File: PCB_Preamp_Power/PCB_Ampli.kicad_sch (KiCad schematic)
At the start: 0 parts

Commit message: PCBV3_Preamp_Power
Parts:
- added H1, H2, H3, H4: MountingHole_Pad, MountingHole:MountingHole_3.2mm_M3_Pad_Via, symbol Mechanical:MountingHole_Pad
- added J4: Conn_01x02, Connector_AMASS:AMASS_XT60-M_1x02_P7.20mm_Vertical, symbol Connector_Generic:Conn_01x02
- added SW2: SW_Push_DPDT, Library_f:Holes_Switch_DPDT, symbol Switch:SW_Push_DPDT
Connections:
- new net: J4.1 (Pin_1), SW2.2 (B)
- new net: J4.2 (Pin_2), SW2.5 (B)
- new net 10: SW2.6 (C)
- new net 2: SW2.1 (A)
- new net 3: SW2.4 (A)
- new net 5: SW2.3 (C)
- new net GND: H1.1, H2.1, H3.1, H4.1
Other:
- note added: "Mounting Holes"
- note added: "Output"

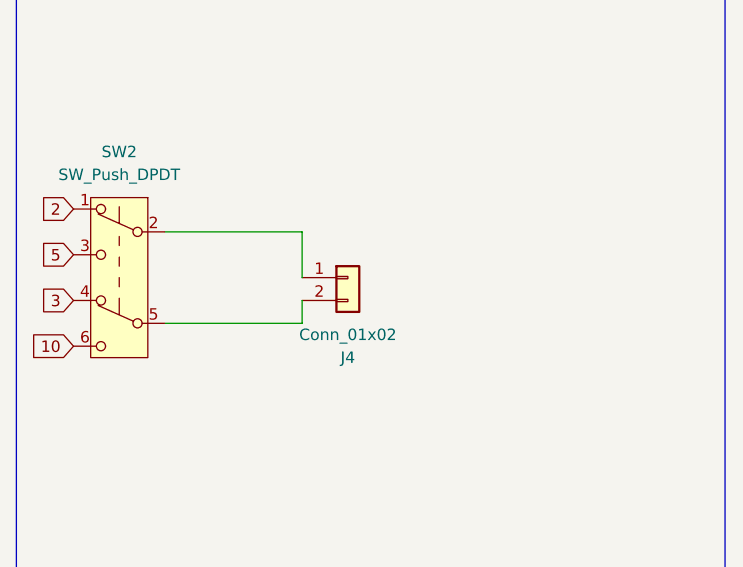
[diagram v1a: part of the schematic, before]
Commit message: PCBV4_Connectors_changed
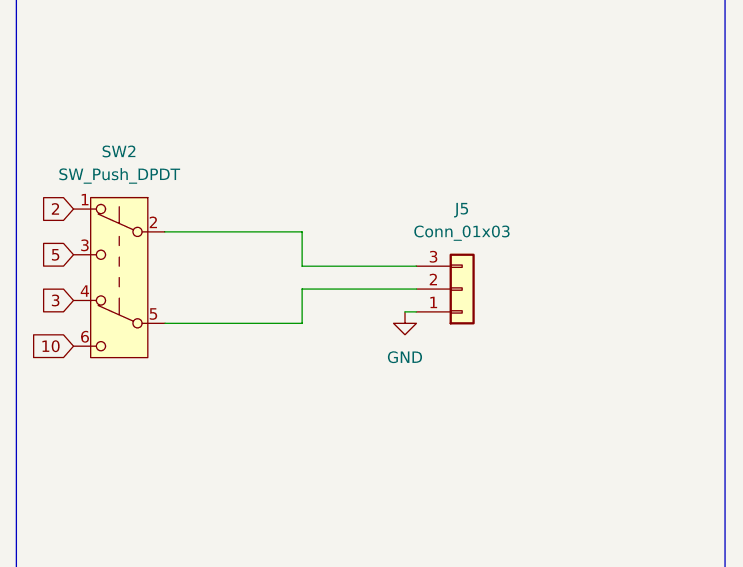
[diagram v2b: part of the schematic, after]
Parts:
- removed J4: Conn_01x02, Connector_AMASS:AMASS_XT60-M_1x02_P7.20mm_Vertical, symbol Connector_Generic:Conn_01x02
- added J5: Conn_01x03, Connector_JST:JST_EH_B3B-EH-A_1x03_P2.50mm_Vertical, symbol Connector_Generic:Conn_01x03
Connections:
- net GND: now also J5.1 (Pin_1)
- net at SW2.2 (B): now also J5.3 (Pin_3)
- net at SW2.5 (B): now also J5.2 (Pin_2)
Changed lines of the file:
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@@
-	(wire
-		(pts
-			(xy 233.68 66.04) (xy 233.68 63.5)
-		)
-		(stroke
-			(width 0)
-			(type default)
-		)
-	)
 	(wire
 		(pts
@@
 	(wire
 		(pts
-			(xy 233.68 55.88) (xy 233.68 60.96)
-		)
-		(stroke
-			(width 0)
-			(type default)
-		)
-	)
-	(wire
-		(pts
 			(xy 218.44 55.88) (xy 233.68 55.88)
 		)
@@
 	(wire
 		(pts
+			(xy 233.68 62.23) (xy 246.38 62.23)
+		)
+		(stroke
+			(width 0)
+			(type default)
+		)
+	)
+	(wire
+		(pts
+			(xy 233.68 66.04) (xy 233.68 62.23)
+		)
+		(stroke
+			(width 0)
+			(type default)
+		)
+	)
+	(wire
+		(pts
 			(xy 247.65 135.89) (xy 247.65 144.78)
+		)
+		(stroke
+			(width 0)
+			(type default)
+		)
+	)
+	(wire
+		(pts
+			(xy 233.68 55.88) (xy 233.68 59.69)
+		)
+		(stroke
+			(width 0)
+			(type default)
+		)
+	)
+	(wire
+		(pts
+			(xy 233.68 59.69) (xy 246.38 59.69)
+		)
+		(stroke
+			(width 0)
+			(type default)
+		)
+	)
+	(wire
+		(pts
+			(xy 246.38 64.77) (xy 245.11 64.77)
 		)
 		(stroke
@@
 	)
 	(symbol
+		(lib_id "Connector_Generic:Conn_01x03")
+		(at 251.46 62.23 0)
+		(mirror x)
+		(unit 1)
+		(exclude_from_sim no)
+		(in_bom yes)
+		(on_board yes)
+		(dnp no)
+		(fields_autoplaced yes)
+		(property "Reference" "J5"
+			(at 251.46 53.34 0)
+			(effects
+				(font
+					(size 1.27 1.27)
+				)
+			)
+		)
+		(property "Value" "Conn_01x03"
+			(at 251.46 55.88 0)
+			(effects
+				(font
+					(size 1.27 1.27)
+				)
+			)
+		)
+		(property "Footprint" "Connector_JST:JST_EH_B3B-EH-A_1x03_P2.50mm_Vertical"
+			(at 251.46 62.23 0)
+			(effects
+				(font
+					(size 1.27 1.27)
+				)
+				(hide yes)
+			)
+		)
+		(property "Datasheet" "~"
+			(at 251.46 62.23 0)
+			(effects
+				(font
+					(size 1.27 1.27)
+				)
+				(hide yes)
+			)
+		)
+		(property "Description" "Generic connector, single row, 01x03, script generated (kicad-library-utils/schlib/autogen/connector/)"
+			(at 251.46 62.23 0)
+			(effects
+				(font
+					(size 1.27 1.27)
+				)
+				(hide yes)
+			)
+		)
+		(pin "2"
+		)
+		(pin "1"
+		)
+		(pin "3"
+		)
+		(instances
+			(project "PCB_Ampli"
+				(path "/3526ba72-9b59-4427-a8d2-8259ce6cbf48"
+					(reference "J5")
+					(unit 1)
+				)
+			)
+		)
+	)
+	(symbol
 		(lib_id "Mechanical:MountingHole_Pad")
 		(at 250.19 152.4 270)
@@
 	)
 	(symbol
-		(lib_id "Connector_Generic:Conn_01x02")
-		(at 238.76 60.96 0)
+		(lib_name "GND_1")
+		(lib_id "power:GND")
+		(at 245.11 64.77 0)
+		(mirror y)
 		(unit 1)
 		(exclude_from_sim no)
@@
 		(on_board yes)
 		(dnp no)
-		(property "Reference" "J4"
-			(at 238.76 69.85 0)
-			(effects
-				(font
-					(size 1.27 1.27)
-				)
-			)
-		)
-		(property "Value" "Conn_01x02"
-			(at 238.76 67.31 0)
-			(effects
-				(font
-					(size 1.27 1.27)
-				)
-			)
-		)
-		(property "Footprint" "Connector_AMASS:AMASS_XT60-M_1x02_P7.20mm_Vertical"
-			(at 238.76 60.96 0)
-			(effects
-				(font
-					(size 1.27 1.27)
-				)
-				(hide yes)
-			)
-		)
-		(property "Datasheet" "~"
-			(at 238.76 60.96 0)
-			(effects
-				(font
-					(size 1.27 1.27)
-				)
-				(hide yes)
-			)
-		)
-		(property "Description" ""
-			(at 238.76 60.96 0)
-			(effects
-				(font
-					(size 1.27 1.27)
-				)
-			)
-		)
-		(pin "2"
+		(fields_autoplaced yes)
+		(property "Reference" "#PWR018"
+			(at 245.11 71.12 0)
+			(effects
+				(font
+					(size 1.27 1.27)
+				)
+				(hide yes)
+			)
+		)
+		(property "Value" "GND"
+			(at 245.11 69.85 0)
+			(effects
+				(font
+					(size 1.27 1.27)
+				)
+			)
+		)
+		(property "Footprint" ""
+			(at 245.11 64.77 0)
+			(effects
+				(font
+					(size 1.27 1.27)
+				)
+				(hide yes)
+			)
+		)
+		(property "Datasheet" ""
+			(at 245.11 64.77 0)
+			(effects
+				(font
+					(size 1.27 1.27)
+				)
+				(hide yes)
+			)
+		)
+		(property "Description" "Power symbol creates a global label with name \"GND\" , ground"
+			(at 245.11 64.77 0)
+			(effects
+				(font
+					(size 1.27 1.27)
+				)
+				(hide yes)
+			)
 		)
 		(pin "1"
@@
 			(project "PCB_Ampli"
 				(path "/3526ba72-9b59-4427-a8d2-8259ce6cbf48"
-					(reference "J4")
+					(reference "#PWR018")
 					(unit 1)
 				)
